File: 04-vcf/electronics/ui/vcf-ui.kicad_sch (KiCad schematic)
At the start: 32 parts, among them J1 Conn_01x04, J2 Conn_02x05_Odd_Even, J3 Conn_02x03_Odd_Even, J4 Conn_01x02, J5 Conn_02x02_Counter_Clockwise, J6 Conn_01x06, U1 0203

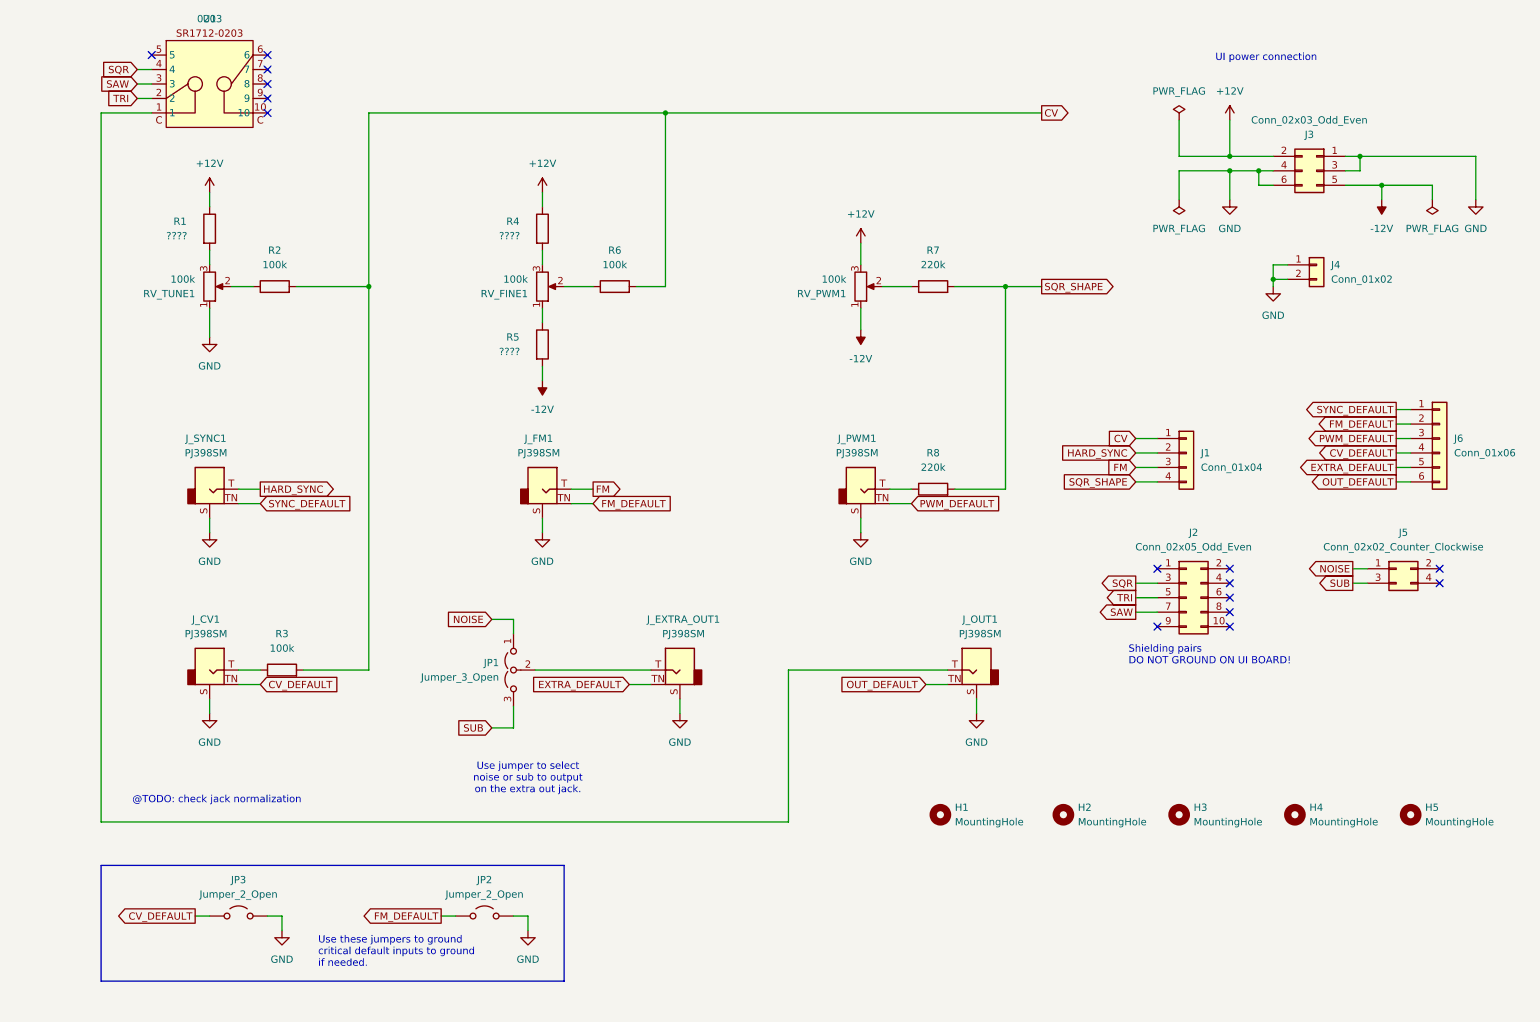
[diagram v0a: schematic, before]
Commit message: Designed UI schematics for VCF
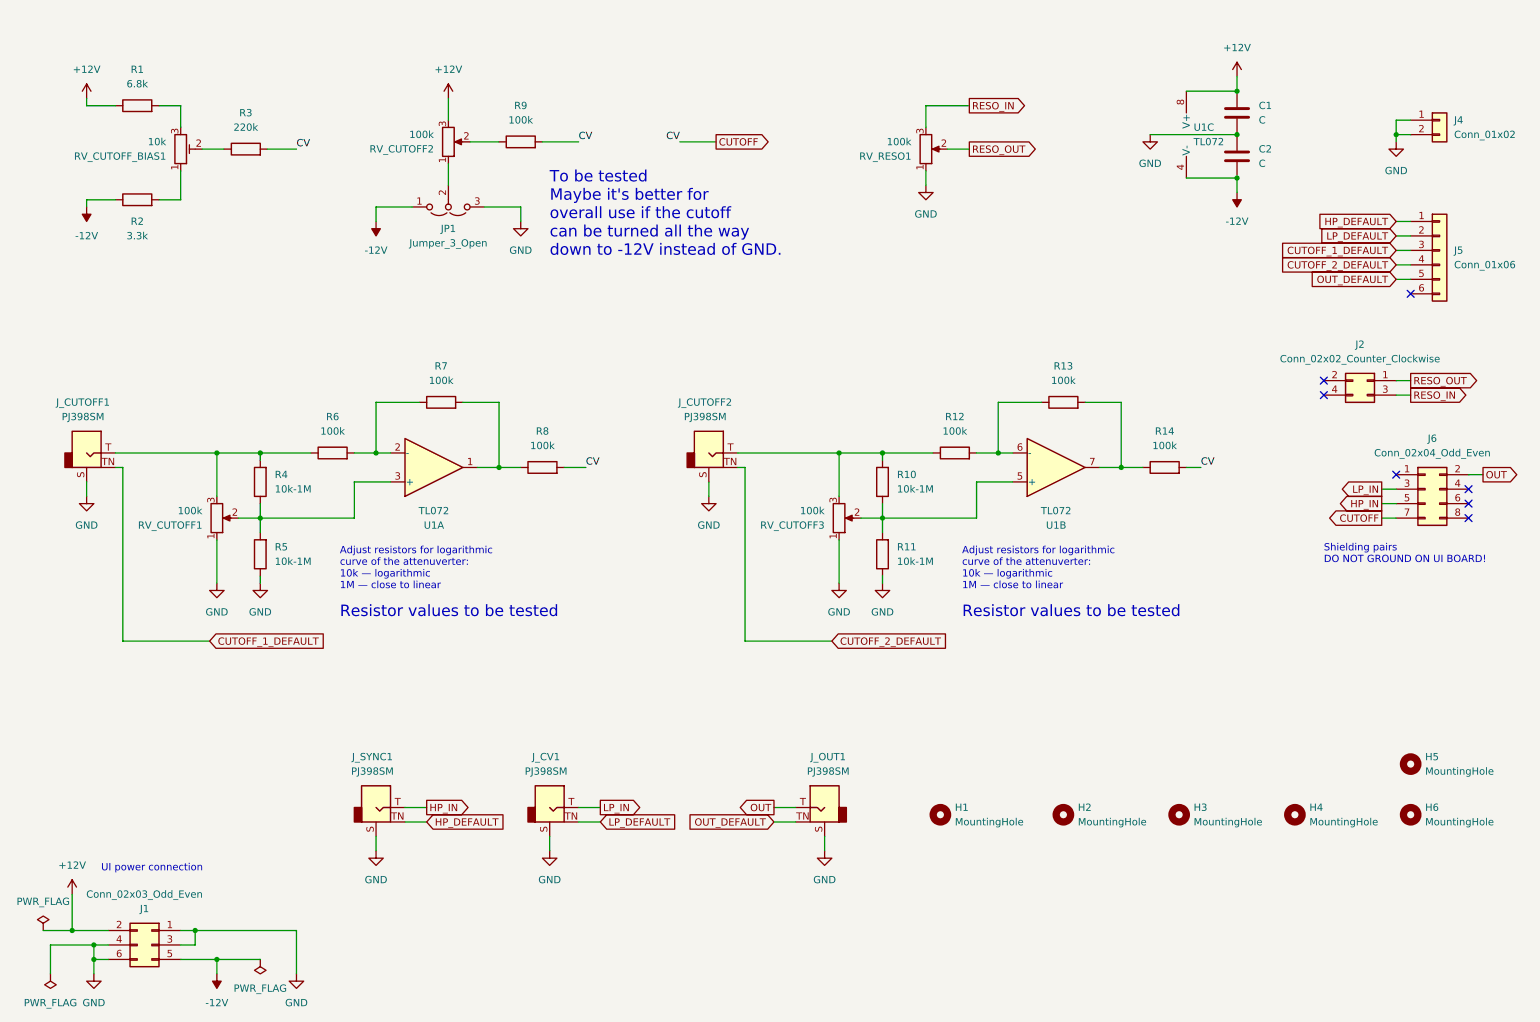
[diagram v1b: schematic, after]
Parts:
- removed J1: Conn_01x04, Connector_PinSocket_2.54mm:PinSocket_1x04_P2.54mm_Vertical, symbol Connector_Generic:Conn_01x04
- removed J2: Conn_02x05_Odd_Even, Connector_PinSocket_2.54mm:PinSocket_2x05_P2.54mm_Vertical, symbol Connector_Generic:Conn_02x05_Odd_Even
- removed JP2, JP3: Jumper_2_Open, Connector_PinHeader_2.54mm:PinHeader_1x02_P2.54mm_Horizontal, symbol Jumper:Jumper_2_Open
- removed J_EXTRA_OUT1, J_PWM1: PJ398SM, Shmoergh_Custom_Footprints:Jack_3.5mm_QingPu_WQP-PJ398SM_Vertical_CircularHoles, symbol Shmoergh-Custom-Components:AudioJack2_Thonkiconn_S
- removed R6: 100k, Shmoergh_Custom_Footprints:R_Axial_DIN0207_L6.3mm_D2.5mm_P7.62mm_Horizontal, symbol Device:R
- removed RV_FINE1: 100k, Shmoergh_Custom_Footprints:Potentiometer_Bourns_Single-PTV09A, symbol Device:R_Potentiometer
- removed U1: 0203, Shmoergh_Custom_Footprints:SR1712-0203, symbol Shmoergh-Custom-Components:SR1712_0203
- added C1, C2: C, Capacitor_THT:C_Disc_D5.0mm_W2.5mm_P2.50mm, symbol Device:C
- added H5: MountingHole, MountingHole:MountingHole_3.2mm_M3_DIN965_Pad, symbol Mechanical:MountingHole
- added J6: Conn_02x04_Odd_Even, Connector_PinSocket_2.54mm:PinSocket_2x04_P2.54mm_Vertical, symbol Connector_Generic:Conn_02x04_Odd_Even
- added J_CUTOFF2: PJ398SM, Shmoergh_Custom_Footprints:Jack_3.5mm_QingPu_WQP-PJ398SM_Vertical_CircularHoles, symbol Shmoergh-Custom-Components:AudioJack2_Thonkiconn_S
- added R10, R11: 10k-1M, Shmoergh_Custom_Footprints:R_Axial_DIN0207_L6.3mm_D2.5mm_P7.62mm_Horizontal, symbol Device:R
- added R12, R13, R14, R7: 100k, Shmoergh_Custom_Footprints:R_Axial_DIN0207_L6.3mm_D2.5mm_P7.62mm_Horizontal, symbol Device:R
- added R2: 3.3k, Shmoergh_Custom_Footprints:R_Axial_DIN0207_L6.3mm_D2.5mm_P7.62mm_Horizontal, symbol Device:R
- added RV_CUTOFF3, RV_RESO1: 100k, Shmoergh_Custom_Footprints:Potentiometer_Bourns_Single-PTV09A, symbol Device:R_Potentiometer
- added RV_CUTOFF_BIAS1: 10k, Shmoergh_Custom_Footprints:Potentiometer_Bourns_Single-PTV09A, symbol Device:R_Potentiometer_Trim
- added U1: TL072, Package_DIP:DIP-8_W7.62mm_LongPads, symbol Amplifier_Operational:TL072
- JP1: footprint Connector_PinHeader_2.54mm:PinHeader_1x03_P2.54mm_Horizontal -> Connector_PinHeader_2.54mm:PinHeader_1x03_P2.54mm_Vertical; Part URL https://mou.sr/451l2py -> (none); Part no. 200-HTSW10308TSRA -> (none); Vendor Mouser -> (none); now left out of the parts list
- R1: value ???? -> 6.8k; Part URL (none) -> https://mou.sr/4hEwI4G; Part no. (none) -> 603-MFR-25FRF52100K
- R3: value 100k -> 220k
- R4, R5: value ???? -> 10k-1M; Part URL (none) -> https://mou.sr/4hEwI4G; Part no. (none) -> 603-MFR-25FRF52100K
- R8: value 220k -> 100k; Part URL https://mou.sr/46cEvF7 -> https://mou.sr/4hEwI4G; Part no. 603-MFR-25FRF52-220K -> 603-MFR-25FRF52100K
- R9: renamed from R7; value 220k -> 100k
- renumbered H5 to H6, J3 to J1, J5 to J2, J6 to J5, J_FM1 to J_CUTOFF1, R2 to R6, RV_TUNE1 to RV_CUTOFF1, RV_PWM1 to RV_CUTOFF2
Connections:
- net EXTRA_DEFAULT is gone; now on net OUT_DEFAULT: J5.5 (Pin_5)
- net FM is gone; now on an unnamed net: J_CUTOFF1.T
- net PWM_DEFAULT is gone; now on net CUTOFF_1_DEFAULT: J5.3 (Pin_3)
- net +12V: now also C1.1, U1.8 (V+); no longer R4.1
- net -12V: now also JP1.1 (A), C2.2, R2.1, U1.4 (V-); no longer R5.2, RV_CUTOFF2.1
- net GND: now also JP1.3 (B), R5.1, C1.2, C2.1, J_CUTOFF2.S, R11.1, RV_CUTOFF3.1, RV_RESO1.1
- net OUT_DEFAULT: no longer J5.6 (Pin_6)
- net at JP1.2 (C): now also RV_CUTOFF2.1
- net at R8.1: now also R7.2, U1.1
- net OUT: now reaches J_OUT1.T
- net OUT: now also J6.2 (Pin_2)
- net at R3.1: now also RV_CUTOFF_BIAS1.2; no longer J_CV1.T
- net at RV_CUTOFF1.3: now also R4.2, R6.1; no longer R1.2
- net at RV_CUTOFF1.2: now also R4.1, R5.2, U1.3 (+); no longer R6.1
- net CV: no longer names the net of R6.2
- net CV: now also R7.1, U1.2 (-); no longer R3.2
- net CV_DEFAULT renamed CUTOFF_2_DEFAULT
- net CUTOFF_2_DEFAULT: now also J_CUTOFF2.TN; no longer J_CV1.TN
- net FM_DEFAULT renamed CUTOFF_1_DEFAULT
- net CUTOFF_1_DEFAULT: no longer J5.2 (Pin_2)
- net HARD_SYNC renamed HP_IN
- net HP_IN: now also J6.5 (Pin_5)
- net NOISE renamed RESO_OUT
- net RESO_OUT: now also RV_RESO1.2; no longer JP1.1 (A)
- net SQR_SHAPE renamed CUTOFF
- net CUTOFF: now also R3.2, J6.7 (Pin_7), R14.2
- net SUB renamed RESO_IN
- net RESO_IN: now also RV_RESO1.3; no longer JP1.3 (B)
- net SYNC_DEFAULT renamed HP_DEFAULT
- new net: R10.1, R11.2, RV_CUTOFF3.2, U1.5 (+)
- new net: J_CUTOFF2.T, R10.2, R12.1, RV_CUTOFF3.3
- new net: R1.2, RV_CUTOFF_BIAS1.3
- new net: R2.2, RV_CUTOFF_BIAS1.1
- new net: R12.2, R13.1, U1.6 (-)
- new net: R13.2, R14.1, U1.7
- new net LP_DEFAULT: J5.2 (Pin_2), J_CV1.TN
- new net LP_IN: J6.3 (Pin_3), J_CV1.T
- no-connect marks 15 -> 7
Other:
- note added: "Adjust resistors for logarithmic curve of the attenuverter: 10k — logarithmic 1M — close to linear"
- note added: "Resistor values to be tested"
- note added: "To be tested Maybe it's better for overall use if the cutoff can be turned all the way down to -12V instead of GND."
- note removed: "@TODO: check jack normalization"
- note removed: "Use jumper to select noise or sub to output on the extra out jack."
- note removed: "Use these jumpers to ground critical default inputs to ground if needed."
- moved on the sheet: J1, J2, J4, J5, J_CUTOFF1, J_CV1, J_OUT1, J_SYNC1, R6, R9, RV_CUTOFF1, RV_CUTOFF2

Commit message: Designed VCF UI board pre-check
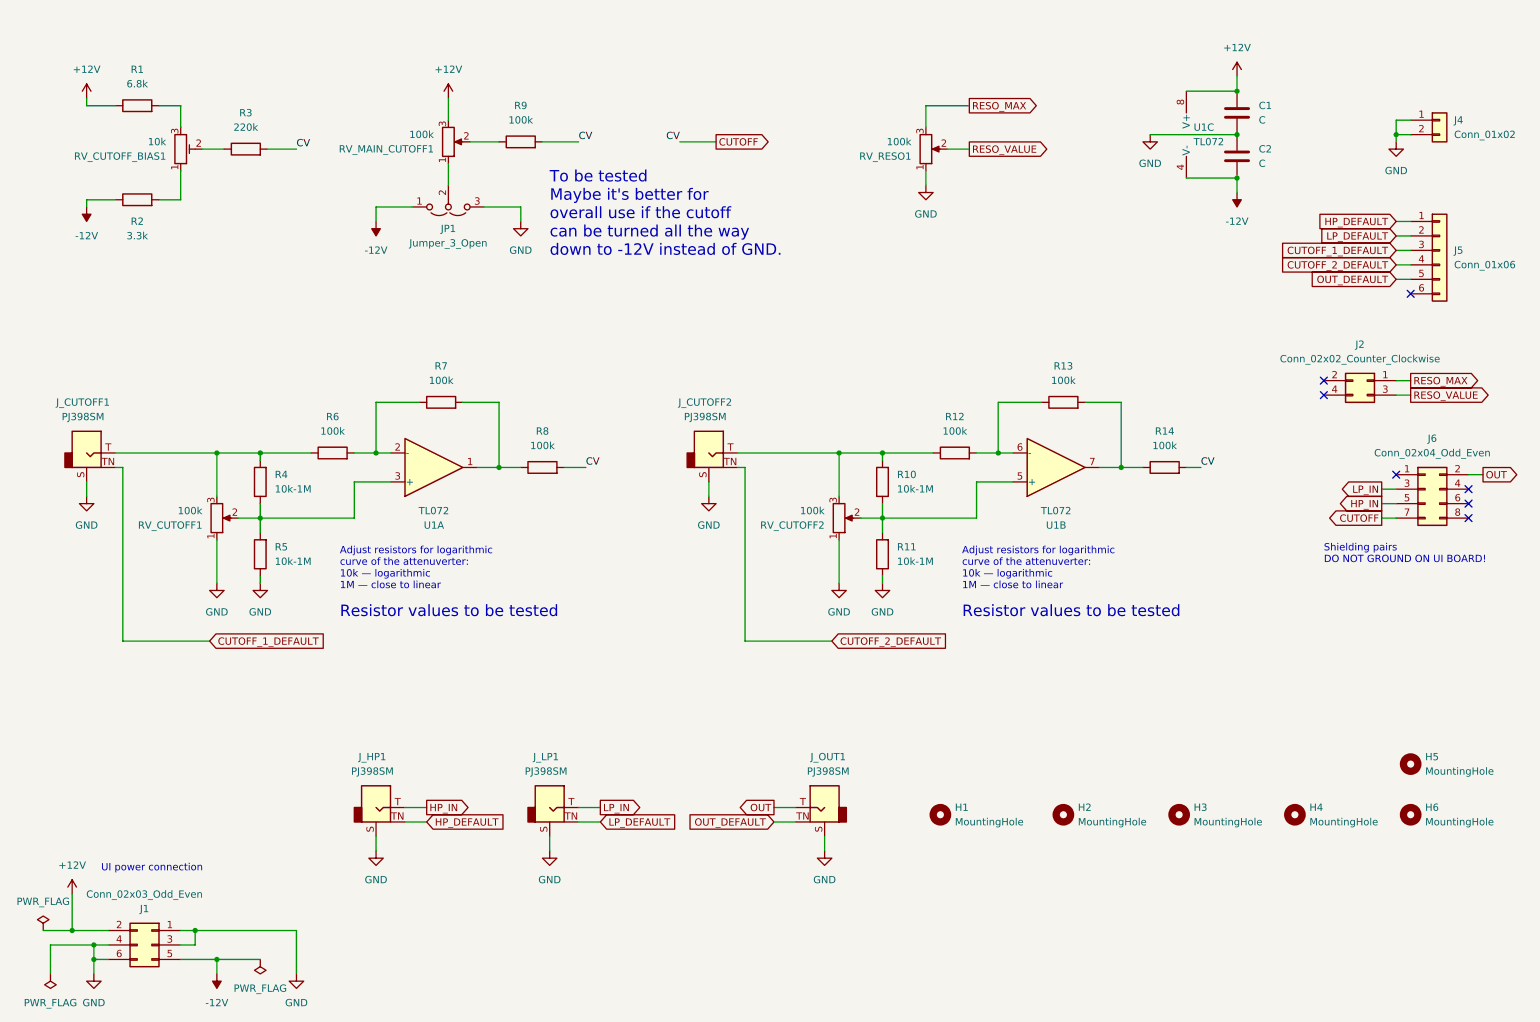
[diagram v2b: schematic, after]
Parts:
- RV_CUTOFF_BIAS1: footprint Shmoergh_Custom_Footprints:Potentiometer_Bourns_Single-PTV09A -> Potentiometer_THT:Potentiometer_ACP_CA6-H2,5_Horizontal
- renumbered J_SYNC1 to J_HP1, J_CV1 to J_LP1, RV_CUTOFF3 to RV_CUTOFF2, RV_CUTOFF2 to RV_MAIN_CUTOFF1
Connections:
- net RESO_IN renamed RESO_MAX
- net RESO_MAX: now also J2.1 (Pin_1); no longer J2.3 (Pin_3)
- net RESO_OUT renamed RESO_VALUE
- net RESO_VALUE: now also J2.3 (Pin_3); no longer J2.1 (Pin_1)
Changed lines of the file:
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@@
 		)
 	)
-	(global_label "RESO_OUT"
+	(global_label "RESO_VALUE"
 		(shape output)
 		(at 184.15 43.18 0)
@@
 		)
 		(property "Intersheetrefs" "${INTERSHEET_REFS}"
-			(at 196.6904 43.18 0)
+			(at 198.7466 43.18 0)
 			(effects
 				(font
@@
 		)
 	)
-	(global_label "RESO_IN"
+	(global_label "RESO_MAX"
 		(shape output)
 		(at 184.15 35.56 0)
@@
 		)
 		(property "Intersheetrefs" "${INTERSHEET_REFS}"
-			(at 194.9971 35.56 0)
+			(at 196.8113 35.56 0)
 			(effects
 				(font
@@
 		)
 	)
-	(global_label "RESO_OUT"
+	(global_label "RESO_MAX"
 		(shape output)
 		(at 261.62 83.82 0)
@@
 		)
 		(property "Intersheetrefs" "${INTERSHEET_REFS}"
-			(at 274.1604 83.82 0)
+			(at 274.2813 83.82 0)
 			(effects
 				(font
@@
 		)
 	)
-	(global_label "RESO_IN"
+	(global_label "RESO_VALUE"
 		(shape output)
 		(at 261.62 86.36 0)
@@
 		)
 		(property "Intersheetrefs" "${INTERSHEET_REFS}"
-			(at 272.4671 86.36 0)
+			(at 276.2166 86.36 0)
 			(effects
 				(font
@@
 		(dnp no)
 		(fields_autoplaced yes)
-		(property "Reference" "J_CV1"
+		(property "Reference" "J_LP1"
 			(at 109.855 149.86 0)
 			(effects
@@
 			(project "vco-ui"
 				(path "/ab333f71-eefa-415f-b212-ebe7a942b1c8"
-					(reference "J_CV1")
+					(reference "J_LP1")
 					(unit 1)
 				)
@@
 		(dnp no)
 		(fields_autoplaced yes)
-		(property "Reference" "J_SYNC1"
+		(property "Reference" "J_HP1"
 			(at 79.375 149.86 0)
 			(effects
@@
 			(project ""
 				(path "/ab333f71-eefa-415f-b212-ebe7a942b1c8"
-					(reference "J_SYNC1")
+					(reference "J_HP1")
 					(unit 1)
 				)
@@
 			)
 		)
-		(property "Footprint" "Shmoergh_Custom_Footprints:Potentiometer_Bourns_Single-PTV09A"
+		(property "Footprint" "Potentiometer_THT:Potentiometer_ACP_CA6-H2,5_Horizontal"
 			(at 45.72 43.18 0)
 			(effects
@@
 			)
 		)
+		(property "Part No." ""
+			(at 45.72 43.18 0)
+			(effects
+				(font
+					(size 1.27 1.27)
+				)
+				(hide yes)
+			)
+		)
+		(property "Part URL" ""
+			(at 45.72 43.18 0)
+			(effects
+				(font
+					(size 1.27 1.27)
+				)
+				(hide yes)
+			)
+		)
+		(property "Vendor" ""
+			(at 45.72 43.18 0)
+			(effects
+				(font
+					(size 1.27 1.27)
+				)
+				(hide yes)
+			)
+		)
+		(property "LCSC" ""
+			(at 45.72 43.18 0)
+			(effects
+				(font
+					(size 1.27 1.27)
+				)
+				(hide yes)
+			)
+		)
 		(pin "1"
 		)
@@
 		(on_board yes)
 		(dnp no)
-		(property "Reference" "RV_CUTOFF3"
+		(property "Reference" "RV_CUTOFF2"
 			(at 158.75 109.2201 0)
 			(effects
@@
 			(project "vcf-ui"
 				(path "/ab333f71-eefa-415f-b212-ebe7a942b1c8"
-					(reference "RV_CUTOFF3")
+					(reference "RV_CUTOFF2")
 					(unit 1)
 				)
@@
 		(on_board yes)
 		(dnp no)
-		(property "Reference" "RV_CUTOFF2"
+		(property "Reference" "RV_MAIN_CUTOFF1"
 			(at 90.17 43.1801 0)
 			(effects
@@
 			(project "vco-ui"
 				(path "/ab333f71-eefa-415f-b212-ebe7a942b1c8"
-					(reference "RV_CUTOFF2")
+					(reference "RV_MAIN_CUTOFF1")
 					(unit 1)
 				)
